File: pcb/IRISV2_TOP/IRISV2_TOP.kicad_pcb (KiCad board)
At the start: 6 copper layers, 50 x 50 mm, 155 parts, among them IC1 ATA6561-GAQW-N, IC2 S25FL256LAGNFI010, IC3 STM32C552MET6, J1 Conn_01x20_MountingPin, J10 Conn_02x15_Odd_Even, J11 Conn_01x04_MountingPin, J12 Conn_01x04_MountingPin, J2 Conn_02x03_Odd_Even, J3 Conn_01x03, J4 Conn_01x02, J5 Conn_02x15_Odd_Even, J6 MEM2085-00-115-00-A, J7 Conn_Coaxial, J8 Conn_Coaxial, J9 Conn_01x06_MountingPin, U4 STM32H563VITx, U5 MMC5983MA, U6 ICM-45686, U7 ICM-45686, U8 BMP581, U9 lr2021, Y1 25mHz 8pf, Y2 32.768kHz 12.5pF, Y3 24mHz 8pf, Y4 32.768kHz 12.5pF

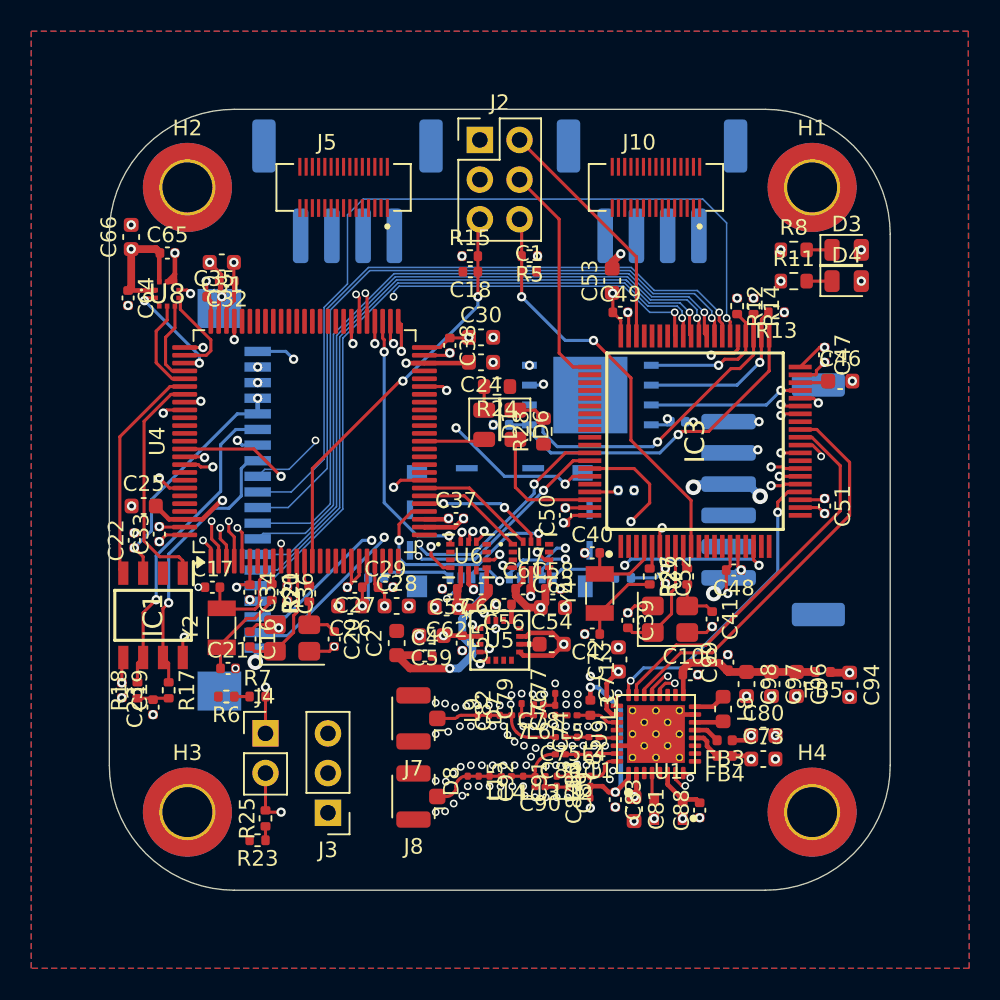
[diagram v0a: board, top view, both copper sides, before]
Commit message: 3d models nearly done, just missing a few, gpio header routed - about to change lr2021 trace width
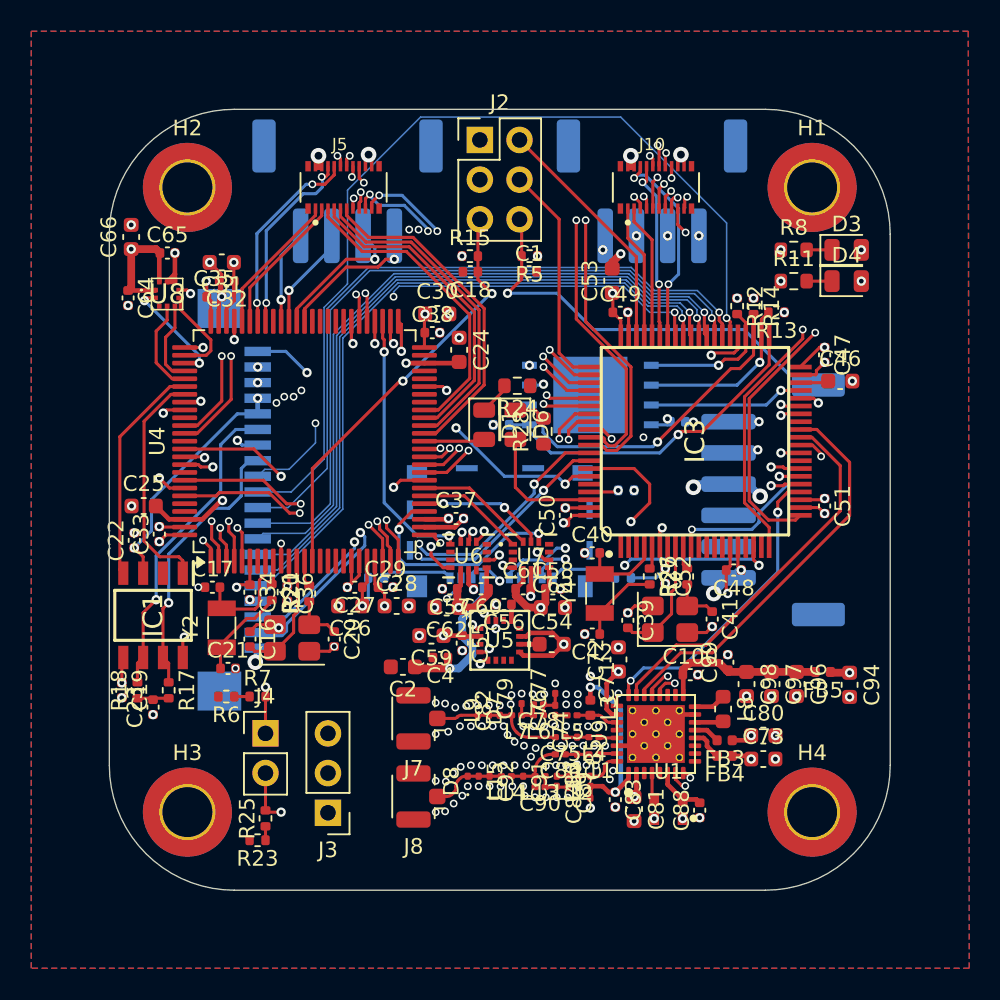
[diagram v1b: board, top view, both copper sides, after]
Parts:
- J10, J5: value Conn_02x15_Odd_Even -> Conn_02x10_Odd_Even_MountingPin; footprint 10164227-0304A1RLF:AMPHENOL_10164227-0305A1RLF -> 10164228-0201A1RLF:AMPHENOL_10164228-0201A1RLF
- moved C30 3.18 mm to (146.0, 88.1)
- moved C24 1.61 mm to (147.4, 90.4), turned to -90 degrees
- moved C2 1.58 mm to (143.8, 110.7), turned to 180 degrees
- moved C38 1.39 mm to (145.7, 89.3), turned to 0 degrees
- moved R24 1.30 mm to (151.1, 92.7)
- moved C4 1.00 mm to (146.2, 110.1), turned to 180 degrees
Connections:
- IC3 pad 20: ppu_usart2_tx -> /peripheral_mcu/usart2_tx
- IC3 pad 21: ppu_usart2_rx -> /peripheral_mcu/usart2_rx
- IC3 pad 54: ppu_usart1_tx -> /peripheral_mcu/usart1_tx
- IC3 pad 55: ppu_usart1_rx -> /peripheral_mcu/usart1_rx
- IC3 pad 56: usb2_d- -> /peripheral_mcu/usb_d-
- IC3 pad 57: usb2_d+ -> /peripheral_mcu/usb_d+
- IC3 pad 62: unconnected-(IC3-PA15-Pad62) -> /peripheral_mcu/gpio0
- IC3 pad 63: unconnected-(IC3-PC10-Pad63) -> /peripheral_mcu/gpio1
- IC3 pad 64: unconnected-(IC3-PC11-Pad64) -> /peripheral_mcu/gpio2
- IC3 pad 65: unconnected-(IC3-PC12-Pad65) -> /peripheral_mcu/gpio3
- IC3 pad 66: unconnected-(IC3-PD0-Pad66) -> /peripheral_mcu/gpio4
- IC3 pad 67: unconnected-(IC3-PD1-Pad67) -> /peripheral_mcu/gpio5
- IC3 pad 68: unconnected-(IC3-PD2-Pad68) -> /peripheral_mcu/gpio6
- IC3 pad 69: /peripheral_mcu/swo -> /peripheral_mcu/gpio7/swo
- IC3 pad 70: unconnected-(IC3-PB4-Pad70) -> /peripheral_mcu/i2c1_scl
- IC3 pad 71: unconnected-(IC3-PB5-Pad71) -> /peripheral_mcu/i2c1_sda
- J10 pad 1: unconnected-(J10-Pin_1-Pad1) -> /peripheral_mcu/usb_d+
- J10 pad 10: unconnected-(J10-Pin_10-Pad10) -> /peripheral_mcu/usart2_tx
- J10 pad 11: unconnected-(J10-Pin_11-Pad11) -> /peripheral_mcu/gpio3
- J10 pad 12: unconnected-(J10-Pin_12-Pad12) -> /peripheral_mcu/usart2_rx
- J10 pad 13: unconnected-(J10-Pin_13-Pad13) -> /peripheral_mcu/gpio4
- J10 pad 14: unconnected-(J10-Pin_14-Pad14) -> /peripheral_mcu/i2c1_sda
- J10 pad 15: unconnected-(J10-Pin_15-Pad15) -> /peripheral_mcu/gpio5
- J10 pad 16: unconnected-(J10-Pin_16-Pad16) -> /peripheral_mcu/i2c1_scl
- J10 pad 17: unconnected-(J10-Pin_17-Pad17) -> /peripheral_mcu/gpio6
- J10 pad 18: unconnected-(J10-Pin_18-Pad18) -> GND
- J10 pad 19: unconnected-(J10-Pin_19-Pad19) -> /peripheral_mcu/gpio7/swo
- J10 pad 2: unconnected-(J10-Pin_2-Pad2) -> +3.3V
- J10 pad 20: unconnected-(J10-Pin_20-Pad20) -> GND
- J10 pad 3: unconnected-(J10-Pin_3-Pad3) -> /peripheral_mcu/usb_d-
- J10 pad 4: unconnected-(J10-Pin_4-Pad4) -> +3.3V
- J10 pad 5: unconnected-(J10-Pin_5-Pad5) -> /peripheral_mcu/gpio0
- J10 pad 6: unconnected-(J10-Pin_6-Pad6) -> /peripheral_mcu/usart1_tx
- J10 pad 7: unconnected-(J10-Pin_7-Pad7) -> /peripheral_mcu/gpio1
- J10 pad 8: unconnected-(J10-Pin_8-Pad8) -> /peripheral_mcu/usart1_rx
- J10 pad 9: unconnected-(J10-Pin_9-Pad9) -> /peripheral_mcu/gpio2
- J11 pad 1: /main_mcu/pwm1 -> /main_mcu/pwm4
- J11 pad 2: /main_mcu/pwm2 -> /main_mcu/pwm3
- J11 pad 3: /main_mcu/pwm3 -> /main_mcu/pwm2
- J11 pad 4: /main_mcu/pwm4 -> /main_mcu/pwm1
- J12 pad 1: /main_mcu/pwm5 -> /main_mcu/pwm8
- J12 pad 2: /main_mcu/pwm6 -> /main_mcu/pwm7
- J12 pad 3: /main_mcu/pwm7 -> /main_mcu/pwm6
- J12 pad 4: /main_mcu/pwm8 -> /main_mcu/pwm5
- J5 pad 1: unconnected-(J5-Pin_1-Pad1) -> /main_mcu/usb_d+
- J5 pad 10: unconnected-(J5-Pin_10-Pad10) -> /main_mcu/usart2_tx
- J5 pad 11: unconnected-(J5-Pin_11-Pad11) -> /main_mcu/gpio4
- J5 pad 12: unconnected-(J5-Pin_12-Pad12) -> /main_mcu/usart2_rx
- J5 pad 13: unconnected-(J5-Pin_13-Pad13) -> /main_mcu/gpio3
- J5 pad 14: unconnected-(J5-Pin_14-Pad14) -> /main_mcu/i2c1_sda
- J5 pad 15: unconnected-(J5-Pin_15-Pad15) -> /main_mcu/gpio2
- J5 pad 16: unconnected-(J5-Pin_16-Pad16) -> /main_mcu/i2c1_scl
- J5 pad 17: unconnected-(J5-Pin_17-Pad17) -> /main_mcu/gpio1
- J5 pad 18: unconnected-(J5-Pin_18-Pad18) -> GND
- J5 pad 19: unconnected-(J5-Pin_19-Pad19) -> /main_mcu/gpio0
- J5 pad 2: unconnected-(J5-Pin_2-Pad2) -> +3.3V
- J5 pad 20: unconnected-(J5-Pin_20-Pad20) -> GND
- J5 pad 3: unconnected-(J5-Pin_3-Pad3) -> /main_mcu/usb_d-
- J5 pad 4: unconnected-(J5-Pin_4-Pad4) -> +3.3V
- J5 pad 5: unconnected-(J5-Pin_5-Pad5) -> /main_mcu/gpio7
- J5 pad 6: unconnected-(J5-Pin_6-Pad6) -> /main_mcu/usart1_tx
- J5 pad 7: unconnected-(J5-Pin_7-Pad7) -> /main_mcu/gpio6
- J5 pad 8: unconnected-(J5-Pin_8-Pad8) -> /main_mcu/usart1_rx
- J5 pad 9: unconnected-(J5-Pin_9-Pad9) -> /main_mcu/gpio5
- U4 pad 34: unconnected-(U4-PC5-Pad34) -> /main_mcu/gpio0
- U4 pad 35: unconnected-(U4-PB0-Pad35) -> /main_mcu/gpio1
- U4 pad 36: unconnected-(U4-PB1-Pad36) -> /main_mcu/gpio2
- U4 pad 37: unconnected-(U4-PB2-Pad37) -> /main_mcu/gpio3
- U4 pad 39: unconnected-(U4-PE8-Pad39) -> /main_mcu/gpio4
- U4 pad 40: unconnected-(U4-PE9-Pad40) -> /main_mcu/gpio5
- U4 pad 41: unconnected-(U4-PE10-Pad41) -> /main_mcu/gpio6
- U4 pad 42: unconnected-(U4-PE11-Pad42) -> /main_mcu/gpio7
- U4 pad 43: unconnected-(U4-PE12-Pad43) -> /main_mcu/gpio8
- U4 pad 44: unconnected-(U4-PE13-Pad44) -> /main_mcu/gpio9
- U4 pad 46: unconnected-(U4-PE15-Pad46) -> /main_mcu/gpio10
- U4 pad 47: unconnected-(U4-PB10-Pad47) -> /main_mcu/gpio11
- U4 pad 58: mpu_uart4_rx -> unconnected-(U4-PD11-Pad58)
- U4 pad 59: mpu_uart4_tx -> unconnected-(U4-PD12-Pad59)
- U4 pad 68: /main_mcu/debug_uart_tx -> /main_mcu/usart1_tx
- U4 pad 69: /main_mcu/debug_uart_rx -> /main_mcu/usart1_rx
- U4 pad 70: usb1_d- -> /main_mcu/usb_d-
- U4 pad 71: usb1_d+ -> /main_mcu/usb_d+
- U4 pad 86: mpu_usart2_tx -> /main_mcu/usart2_tx
- U4 pad 87: mpu_usart2_rx -> /main_mcu/usart2_rx
- U4 pad 93: mpu_i2c1_sda -> /main_mcu/i2c1_sda
- U4 pad 95: mpu_i2c1_scl -> /main_mcu/i2c1_scl
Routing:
- net /main_mcu/pwm5: track 0.00 -> 47.7 mm, vias 0 -> 3
- net /main_mcu/pwm6: track 0.00 -> 45.0 mm, vias 0 -> 3
- net /main_mcu/pwm8: track 0.00 -> 44.1 mm, vias 0 -> 3
- net /main_mcu/pwm7: track 0.00 -> 42.0 mm, vias 0 -> 3
- net /main_mcu/i2c1_scl: track 0.00 -> 40.3 mm, vias 0 -> 2
- net /main_mcu/i2c1_sda: track 0.00 -> 36.8 mm, vias 0 -> 2
- net /peripheral_mcu/usart2_rx: track 0.00 -> 34.3 mm, vias 0 -> 2
- net /peripheral_mcu/i2c1_scl: track 0.00 -> 33.9 mm, vias 0 -> 2
- net /peripheral_mcu/usart2_tx: track 0.00 -> 32.7 mm, vias 0 -> 2
- net /peripheral_mcu/i2c1_sda: track 0.00 -> 29.5 mm, vias 0 -> 2
- net /peripheral_mcu/gpio5: track 0.00 -> 25.3 mm, vias 0 -> 2
- net /main_mcu/gpio0: track 0.00 -> 24.5 mm, vias 0 -> 3
- net /main_mcu/gpio1: track 0.00 -> 23.9 mm, vias 0 -> 3
- net /peripheral_mcu/gpio7/swo: track 0.00 -> 23.7 mm, vias 0 -> 2
- net /main_mcu/usart2_rx: track 0.00 -> 23.4 mm, vias 0 -> 2
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
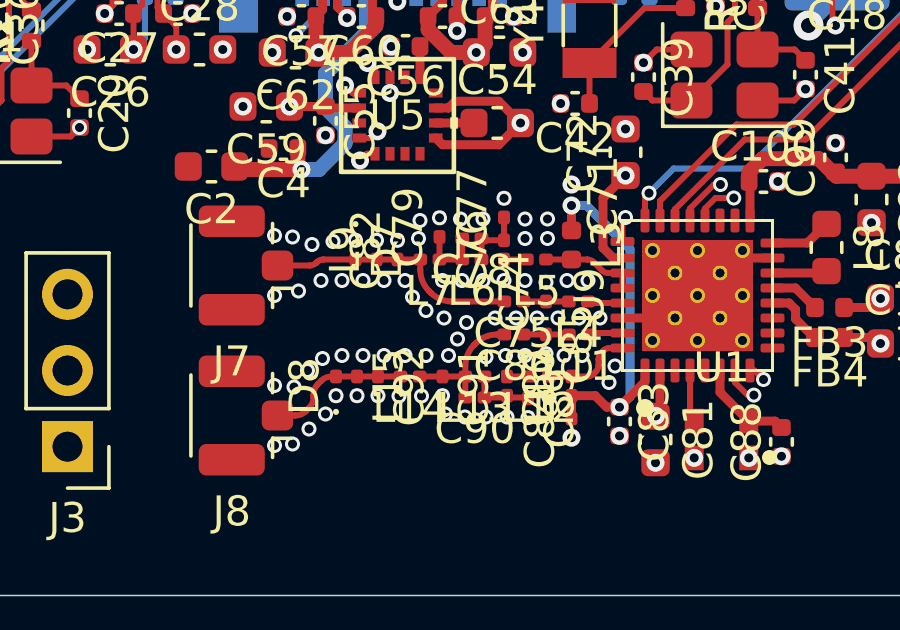
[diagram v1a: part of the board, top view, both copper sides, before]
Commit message: lr2021 trace width changed, with teardrops
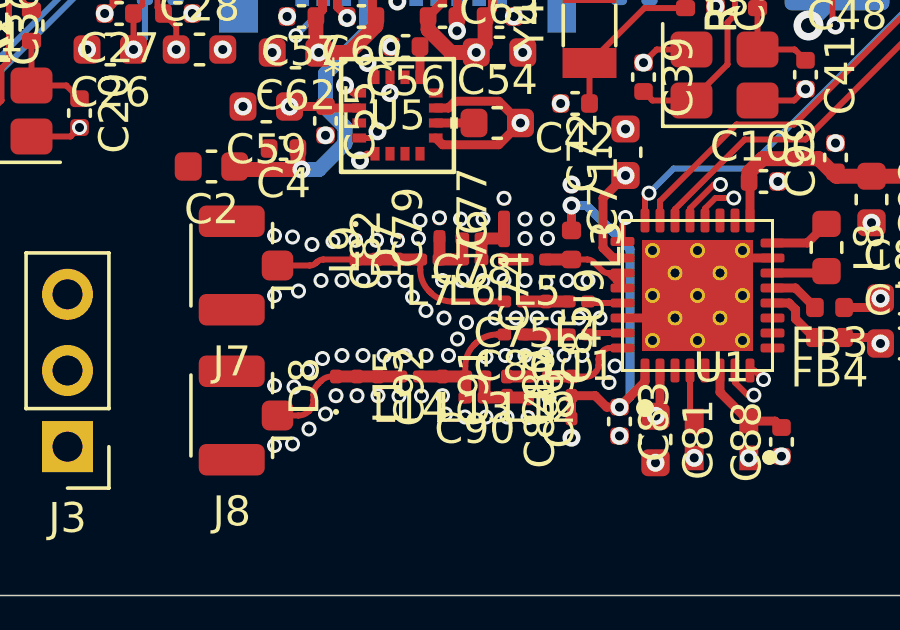
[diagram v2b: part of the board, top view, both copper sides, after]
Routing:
- net /lr2021/lfo: track 3.21 -> 4.26 mm

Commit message: pcb hopefully mostly finalized
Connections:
- J1 pad 1: GND -> cam_uart_tx
- J1 pad 4: GND -> cam_uart_rx
- U4 pad 43: /main_mcu/gpio8 -> unconnected-(U4-PE12-Pad43)
- U4 pad 44: /main_mcu/gpio9 -> unconnected-(U4-PE13-Pad44)
- U4 pad 46: /main_mcu/gpio10 -> unconnected-(U4-PE15-Pad46)
- U4 pad 58: unconnected-(U4-PD11-Pad58) -> cam_uart_rx
- U4 pad 59: unconnected-(U4-PD12-Pad59) -> cam_uart_tx
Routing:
- net cam_uart_tx: track 0.00 -> 25.9 mm, vias 0 -> 2
- net cam_uart_rx: track 0.00 -> 21.4 mm, vias 0 -> 2
- net GND: track 61.2 -> 63.9 mm, vias 150 -> 148
- net /main_mcu/i2c1_scl: track 40.3 -> 39.0 mm
- net /main_mcu/i2c1_sda: track 36.8 -> 37.9 mm
